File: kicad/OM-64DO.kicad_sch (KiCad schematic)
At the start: 21 parts, among them J101 PT 1,5/4-3,5-H, J102 02x03 1.27, U101 R-78E3.3-1.0, U102 THVD1450DRBR, U103 STM32G031F8P6

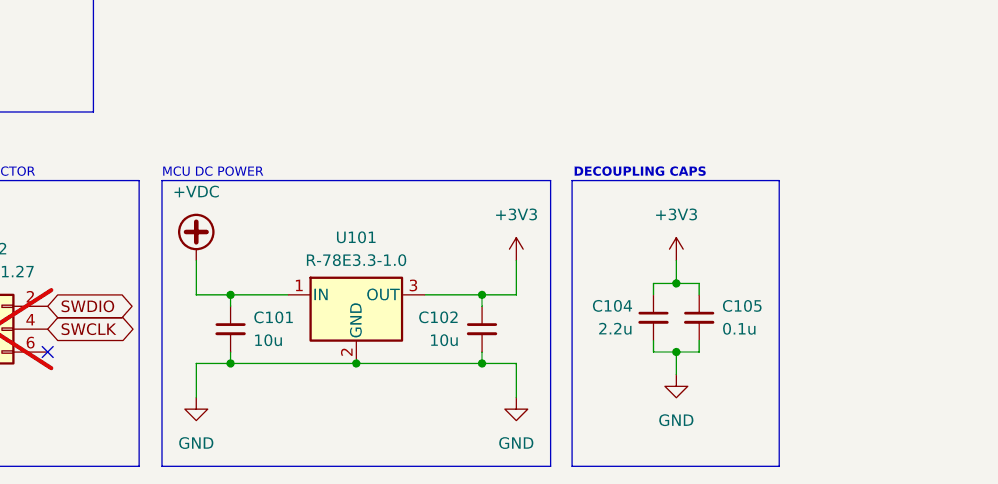
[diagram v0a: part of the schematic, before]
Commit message: feat: add power indicator, add STM32 code
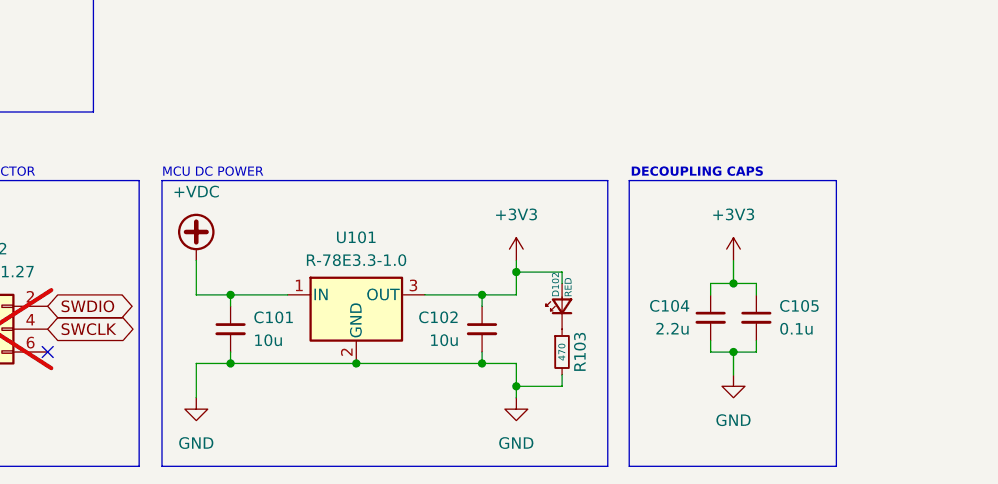
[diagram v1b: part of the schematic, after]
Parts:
- added D102: RED, LED_SMD:LED_0603_1608Metric, symbol Device:LED_Small
- added R103: 470, Resistor_SMD:R_0603_1608Metric, symbol Device:R_Small
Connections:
- net +3V3: now also D102.2 (A)
- net GND: now also R103.2
- new net: D102.1 (K), R103.1
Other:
- moved on the sheet: C104, C105

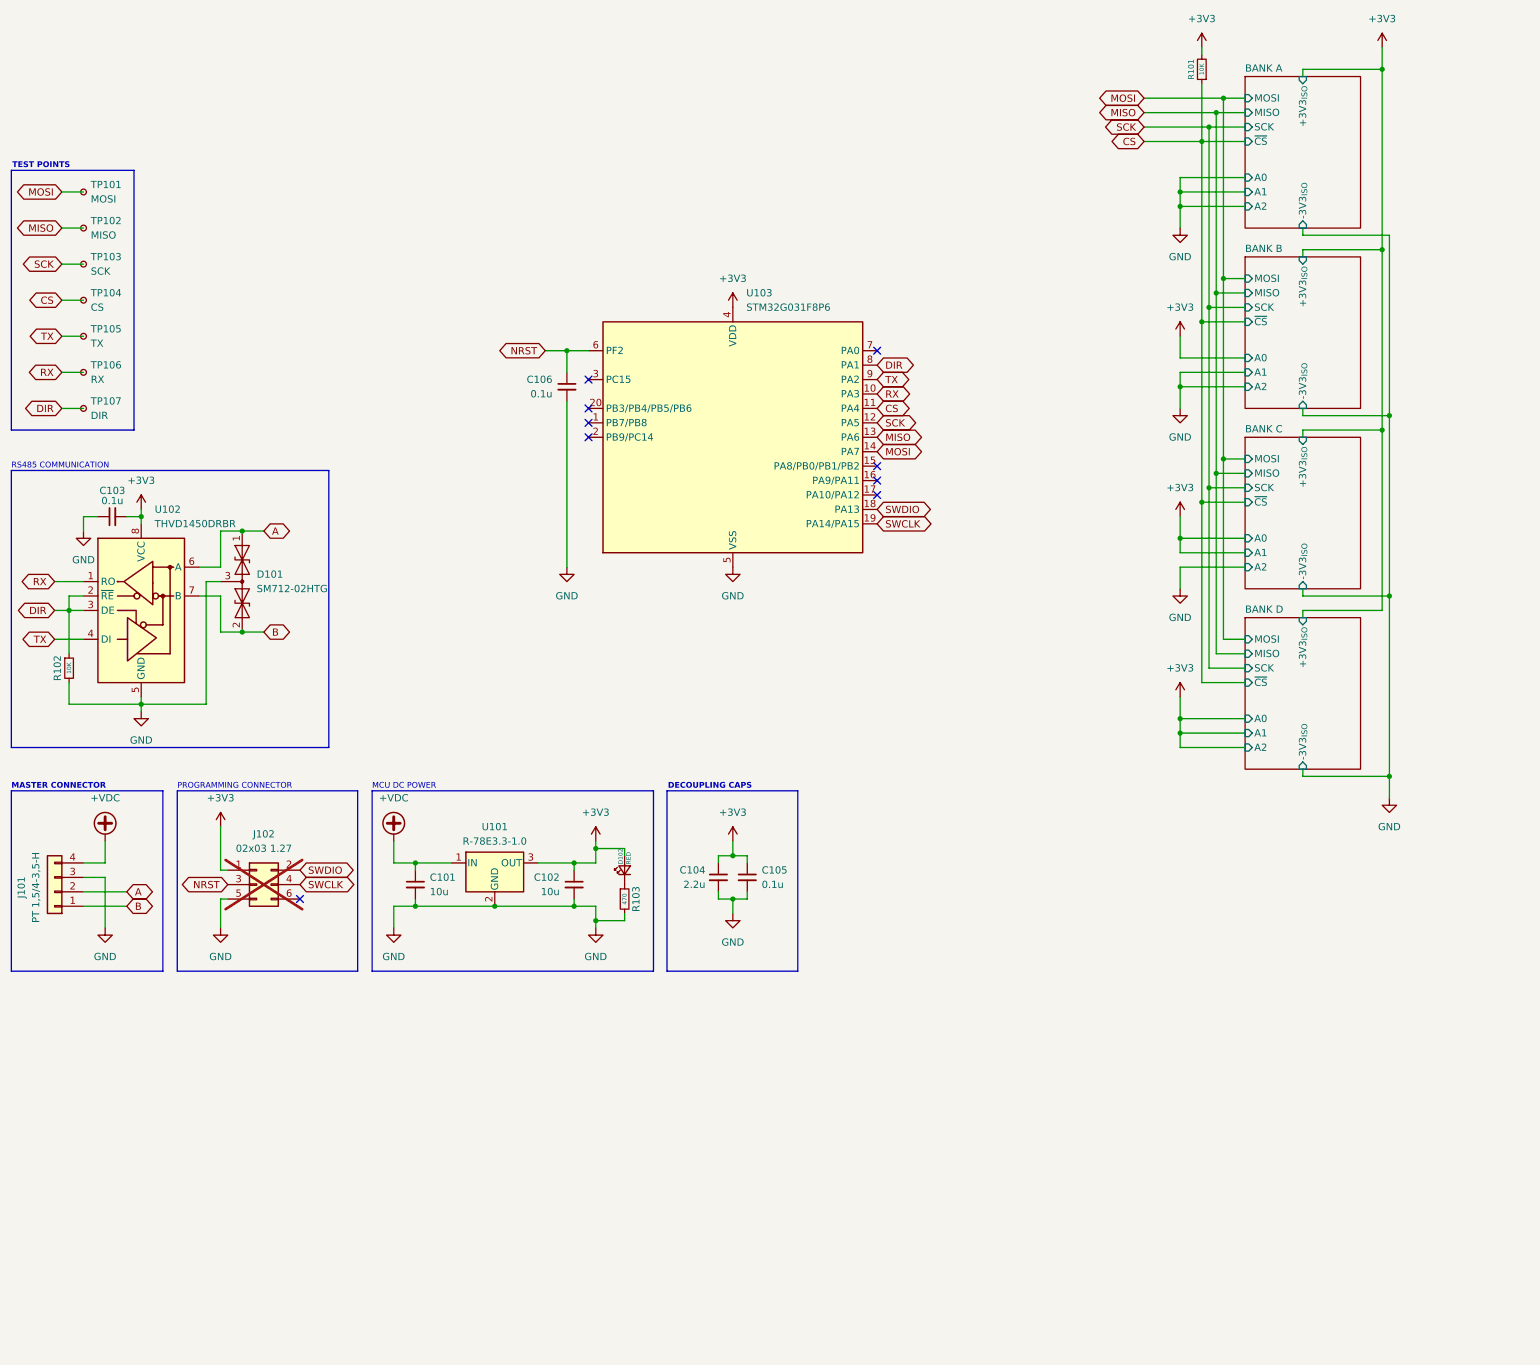
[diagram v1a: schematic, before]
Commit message: feat: add pluggable connector, add JLCPCB production files, improve routing
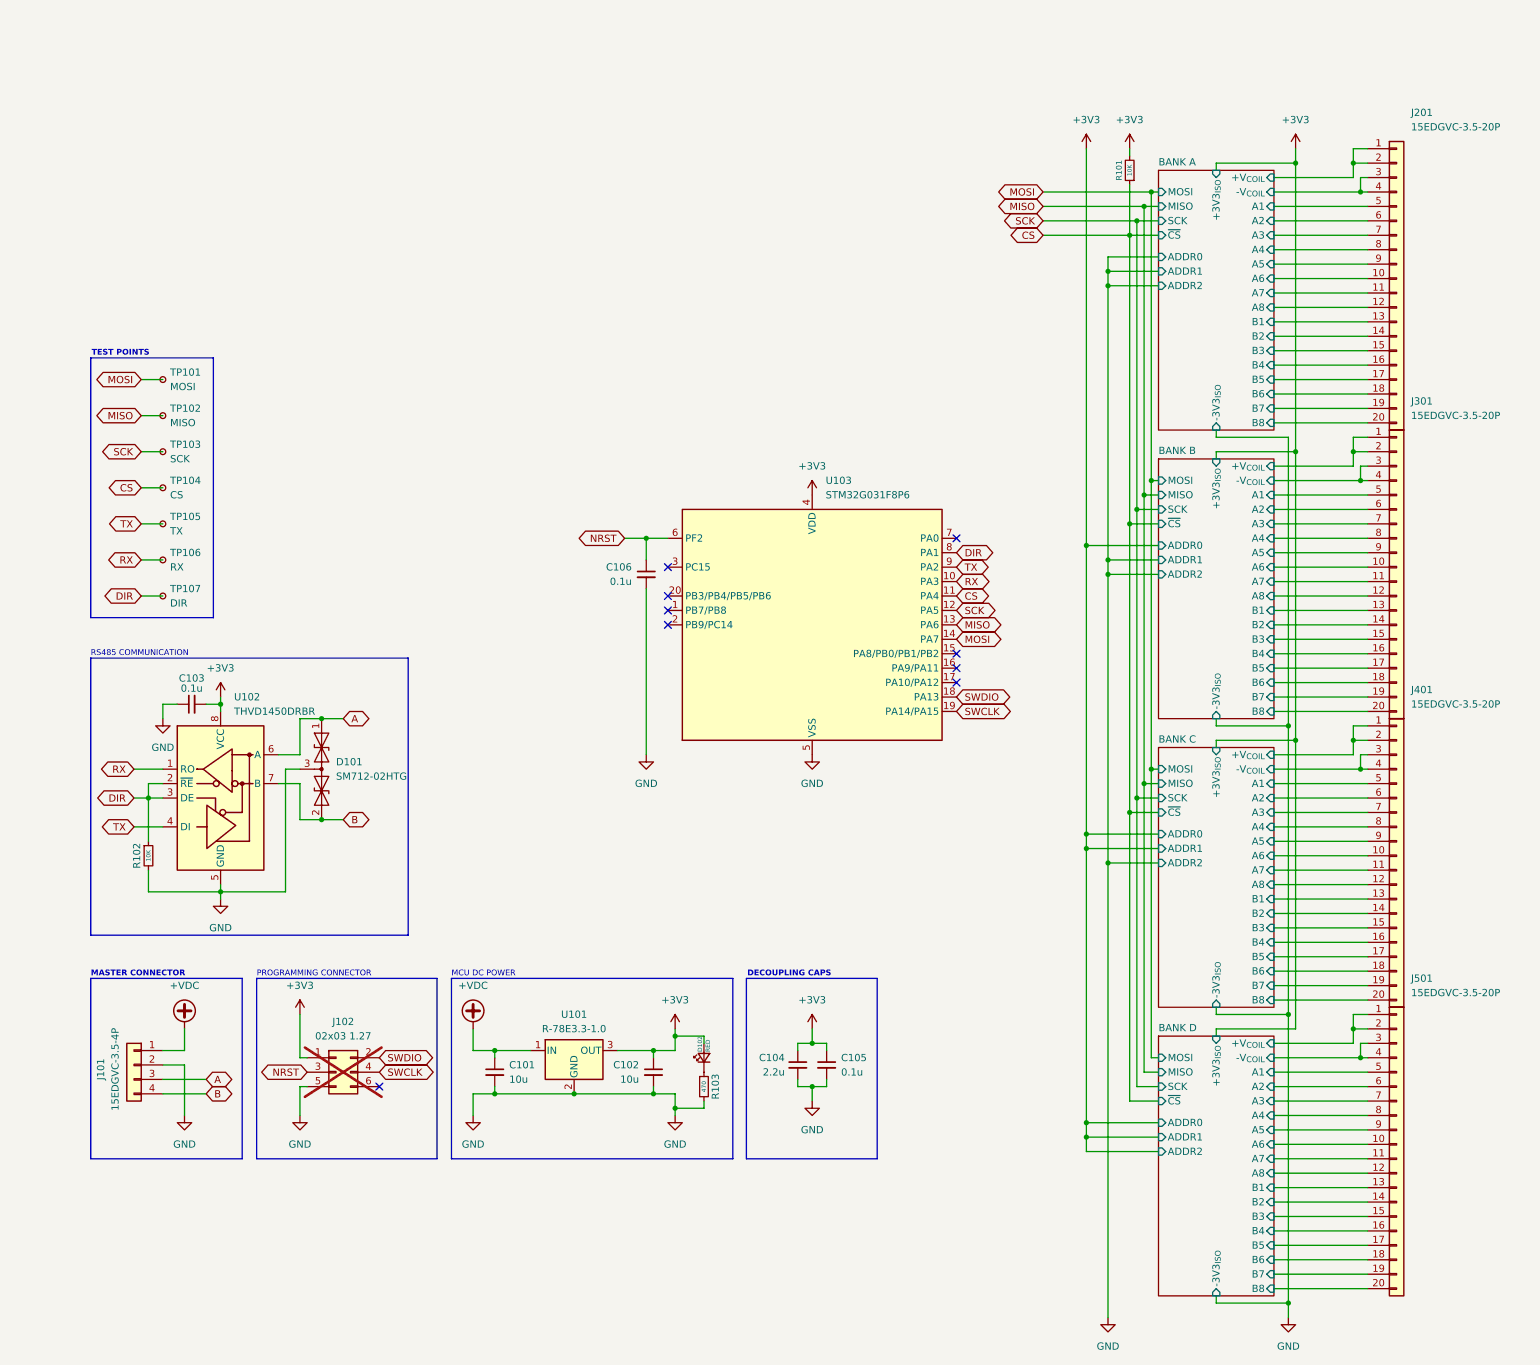
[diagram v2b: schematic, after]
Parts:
- added J201, J301, J401, J501: 15EDGVC-3.5-20P, Project_Library:TerminalBlock_DEGSON_15EDGVC-3.5-20P_No_SilkScreen, symbol Connector_Generic:Conn_01x20
- J101: value PT 1,5/4-3,5-H -> 15EDGVC-3.5-4P; footprint Project_Library:TerminalBlock_Phoenix_PT-1,5-4-3.5-H_1x04_P3.50mm_Horizontal_No_SilkScreen -> Project_Library:TerminalBlock_DEGSON_15EDGVC-3.5-4P_No_SilkScreen; Manufacturer Phoenix Contact -> DEGSON; Mouser Part Number 651-1984633 -> (none); Part Number 1984633 -> 10030000681
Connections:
- net +VDC: now also J101.1 (Pin_1); no longer J101.4 (Pin_4)
- net A: now also J101.3 (Pin_3); no longer J101.2 (Pin_2)
- net B: now also J101.4 (Pin_4); no longer J101.1 (Pin_1)
- net GND: now also J101.2 (Pin_2); no longer J101.3 (Pin_3)
- new net BANK A/+V_{COIL}: J201.1 (Pin_1), J201.2 (Pin_2)
- new net BANK A/-V_{COIL}: J201.3 (Pin_3), J201.4 (Pin_4)
- new net BANK A/A1: J201.5 (Pin_5)
- new net BANK A/A2: J201.6 (Pin_6)
- new net BANK A/A3: J201.7 (Pin_7)
- new net BANK A/A4: J201.8 (Pin_8)
- new net BANK A/A5: J201.9 (Pin_9)
- new net BANK A/A6: J201.10 (Pin_10)
- new net BANK A/A7: J201.11 (Pin_11)
- new net BANK A/A8: J201.12 (Pin_12)
- new net BANK A/B1: J201.13 (Pin_13)
- new net BANK A/B2: J201.14 (Pin_14)
- new net BANK A/B3: J201.15 (Pin_15)
- new net BANK A/B4: J201.16 (Pin_16)
- new net BANK A/B5: J201.17 (Pin_17)
- new net BANK A/B6: J201.18 (Pin_18)
- new net BANK A/B7: J201.19 (Pin_19)
- new net BANK A/B8: J201.20 (Pin_20)
- new net BANK B/+V_{COIL}: J301.1 (Pin_1), J301.2 (Pin_2)
- new net BANK B/-V_{COIL}: J301.3 (Pin_3), J301.4 (Pin_4)
- new net BANK B/A1: J301.5 (Pin_5)
- new net BANK B/A2: J301.6 (Pin_6)
- new net BANK B/A3: J301.7 (Pin_7)
- new net BANK B/A4: J301.8 (Pin_8)
- new net BANK B/A5: J301.9 (Pin_9)
- new net BANK B/A6: J301.10 (Pin_10)
- new net BANK B/A7: J301.11 (Pin_11)
- new net BANK B/A8: J301.12 (Pin_12)
- new net BANK B/B1: J301.13 (Pin_13)
- new net BANK B/B2: J301.14 (Pin_14)
- new net BANK B/B3: J301.15 (Pin_15)
- new net BANK B/B4: J301.16 (Pin_16)
- new net BANK B/B5: J301.17 (Pin_17)
- new net BANK B/B6: J301.18 (Pin_18)
- new net BANK B/B7: J301.19 (Pin_19)
- new net BANK B/B8: J301.20 (Pin_20)
- new net BANK C/+V_{COIL}: J401.1 (Pin_1), J401.2 (Pin_2)
- new net BANK C/-V_{COIL}: J401.3 (Pin_3), J401.4 (Pin_4)
- new net BANK C/A1: J401.5 (Pin_5)
- new net BANK C/A2: J401.6 (Pin_6)
- new net BANK C/A3: J401.7 (Pin_7)
- new net BANK C/A4: J401.8 (Pin_8)
- new net BANK C/A5: J401.9 (Pin_9)
- new net BANK C/A6: J401.10 (Pin_10)
- new net BANK C/A7: J401.11 (Pin_11)
- new net BANK C/A8: J401.12 (Pin_12)
- new net BANK C/B1: J401.13 (Pin_13)
- new net BANK C/B2: J401.14 (Pin_14)
- new net BANK C/B3: J401.15 (Pin_15)
- new net BANK C/B4: J401.16 (Pin_16)
- new net BANK C/B5: J401.17 (Pin_17)
- new net BANK C/B6: J401.18 (Pin_18)
- new net BANK C/B7: J401.19 (Pin_19)
- new net BANK C/B8: J401.20 (Pin_20)
- new net BANK D/+V_{COIL}: J501.1 (Pin_1), J501.2 (Pin_2)
- new net BANK D/-V_{COIL}: J501.3 (Pin_3), J501.4 (Pin_4)
- new net BANK D/A1: J501.5 (Pin_5)
- new net BANK D/A2: J501.6 (Pin_6)
- new net BANK D/A3: J501.7 (Pin_7)
- new net BANK D/A4: J501.8 (Pin_8)
- new net BANK D/A5: J501.9 (Pin_9)
- new net BANK D/A6: J501.10 (Pin_10)
- new net BANK D/A7: J501.11 (Pin_11)
- new net BANK D/A8: J501.12 (Pin_12)
- new net BANK D/B1: J501.13 (Pin_13)
- new net BANK D/B2: J501.14 (Pin_14)
- new net BANK D/B3: J501.15 (Pin_15)
- new net BANK D/B4: J501.16 (Pin_16)
- new net BANK D/B5: J501.17 (Pin_17)
- new net BANK D/B6: J501.18 (Pin_18)
- new net BANK D/B7: J501.19 (Pin_19)
- new net BANK D/B8: J501.20 (Pin_20)
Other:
- sheet BANK A ports: added +V_{COIL}, -V_{COIL}, A3, A4, A5, A6, A7, A8, ADDR0, ADDR1, ADDR2, B1, B2, B3, B4, B5, B6, B7, B8; removed A0
- sheet BANK B ports: added +V_{COIL}, -V_{COIL}, A3, A4, A5, A6, A7, A8, ADDR0, ADDR1, ADDR2, B1, B2, B3, B4, B5, B6, B7, B8; removed A0
- sheet BANK C ports: added +V_{COIL}, -V_{COIL}, A3, A4, A5, A6, A7, A8, ADDR0, ADDR1, ADDR2, B1, B2, B3, B4, B5, B6, B7, B8; removed A0
- sheet BANK D ports: added +V_{COIL}, -V_{COIL}, A3, A4, A5, A6, A7, A8, ADDR0, ADDR1, ADDR2, B1, B2, B3, B4, B5, B6, B7, B8; removed A0
- moved on the sheet: C101, C102, C103, C104, C105, C106, D101, D102, J101, J102, R101, R102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

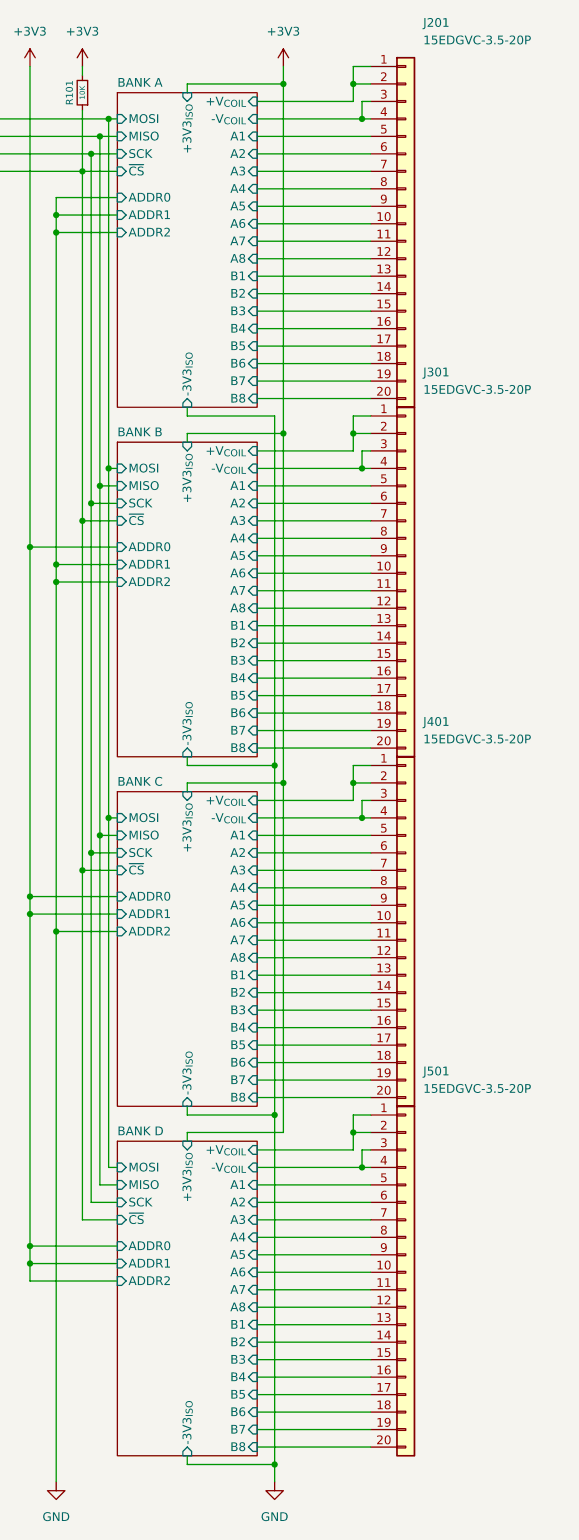
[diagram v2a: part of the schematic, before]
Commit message: fix: wrong silkscreen placement, missing GND <> -V_coil tie
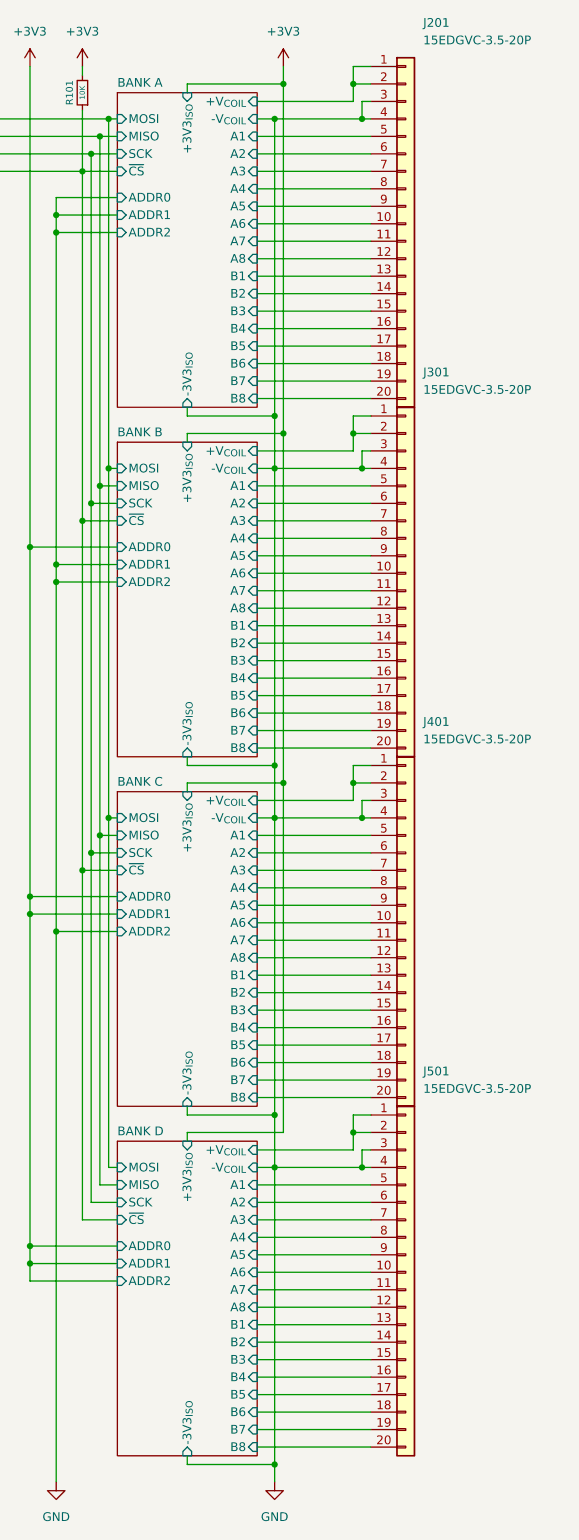
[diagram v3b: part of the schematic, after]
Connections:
- net BANK A/-V_{COIL} is gone; now on net GND: J201.3 (Pin_3), J201.4 (Pin_4)
- net BANK B/-V_{COIL} is gone; now on net GND: J301.3 (Pin_3), J301.4 (Pin_4)
- net BANK C/-V_{COIL} is gone; now on net GND: J401.3 (Pin_3), J401.4 (Pin_4)
- net BANK D/-V_{COIL} is gone; now on net GND: J501.3 (Pin_3), J501.4 (Pin_4)
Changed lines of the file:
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@@
+	)
+	(junction
+		(at 251.46 149.86)
+		(diameter 0)
+		(color 0 0 0 0)
 	)
 	(junction
@@
 	)
 	(junction
+		(at 251.46 91.44)
+		(diameter 0)
+		(color 0 0 0 0)
+	)
+	(junction
 		(at 227.33 48.26)
 		(diameter 0)
@@
 	)
 	(junction
+		(at 251.46 48.26)
+		(diameter 0)
+		(color 0 0 0 0)
+	)
+	(junction
+		(at 251.46 200.66)
+		(diameter 0)
+		(color 0 0 0 0)
+	)
+	(junction
 		(at 215.9 163.83)
 		(diameter 0)
@@
 	(junction
 		(at 264.16 48.26)
+		(diameter 0)
+		(color 0 0 0 0)
+	)
+	(junction
+		(at 251.46 99.06)
 		(diameter 0)
 		(color 0 0 0 0)
@@
 	(wire
 		(pts
-			(xy 251.46 142.24) (xy 251.46 193.04)
+			(xy 251.46 142.24) (xy 251.46 149.86)
 		)
 		(stroke
@@
 	(wire
 		(pts
-			(xy 248.92 200.66) (xy 264.16 200.66)
+			(xy 248.92 200.66) (xy 251.46 200.66)
 		)
 		(stroke
@@
 	(wire
 		(pts
-			(xy 251.46 193.04) (xy 251.46 243.84)
+			(xy 251.46 193.04) (xy 251.46 200.66)
+		)
+		(stroke
+			(width 0)
+			(type default)
+		)
+	)
+	(wire
+		(pts
+			(xy 251.46 200.66) (xy 251.46 243.84)
 		)
 		(stroke
@@
 	(wire
 		(pts
+			(xy 251.46 99.06) (xy 264.16 99.06)
+		)
+		(stroke
+			(width 0)
+			(type default)
+		)
+	)
+	(wire
+		(pts
 			(xy 265.43 93.98) (xy 262.89 93.98)
 		)
@@
 	(wire
 		(pts
-			(xy 248.92 99.06) (xy 264.16 99.06)
+			(xy 248.92 99.06) (xy 251.46 99.06)
 		)
 		(stroke
@@
 	(wire
 		(pts
+			(xy 251.46 48.26) (xy 251.46 91.44)
+		)
+		(stroke
+			(width 0)
+			(type default)
+		)
+	)
+	(wire
+		(pts
 			(xy 238.76 146.05) (xy 238.76 144.78)
 		)
@@
 	(wire
 		(pts
-			(xy 248.92 48.26) (xy 264.16 48.26)
+			(xy 248.92 48.26) (xy 251.46 48.26)
 		)
 		(stroke
@@
 	(wire
 		(pts
+			(xy 251.46 149.86) (xy 251.46 193.04)
+		)
+		(stroke
+			(width 0)
+			(type default)
+		)
+	)
+	(wire
+		(pts
 			(xy 248.92 88.9) (xy 265.43 88.9)
 		)
@@
 	(wire
 		(pts
+			(xy 251.46 99.06) (xy 251.46 142.24)
+		)
+		(stroke
+			(width 0)
+			(type default)
+		)
+	)
+	(wire
+		(pts
 			(xy 143.51 199.39) (xy 139.7 199.39)
 		)
@@
 	(wire
 		(pts
+			(xy 251.46 48.26) (xy 264.16 48.26)
+		)
+		(stroke
+			(width 0)
+			(type default)
+		)
+	)
+	(wire
+		(pts
 			(xy 138.43 109.22) (xy 142.24 109.22)
 		)
@@
 	(wire
 		(pts
+			(xy 251.46 149.86) (xy 264.16 149.86)
+		)
+		(stroke
+			(width 0)
+			(type default)
+		)
+	)
+	(wire
+		(pts
 			(xy 167.64 205.74) (xy 167.64 208.28)
 		)
@@
 	(wire
 		(pts
+			(xy 251.46 200.66) (xy 264.16 200.66)
+		)
+		(stroke
+			(width 0)
+			(type default)
+		)
+	)
+	(wire
+		(pts
 			(xy 165.1 205.74) (xy 165.1 204.47)
 		)
@@
 	(wire
 		(pts
-			(xy 251.46 91.44) (xy 251.46 142.24)
-		)
-		(stroke
-			(width 0)
-			(type default)
-		)
-	)
-	(wire
-		(pts
-			(xy 248.92 149.86) (xy 264.16 149.86)
-		)
-		(stroke
+			(xy 251.46 91.44) (xy 251.46 99.06)
+		)
+		(stroke
+			(width 0)
+			(type default)
+		)
+	)
+	(wire
+		(pts
+			(xy 248.92 149.86) (xy 251.46 149.86)
+		)
+		(stroke
